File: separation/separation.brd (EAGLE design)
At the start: 5 parts, among them IC1 L7805ACV

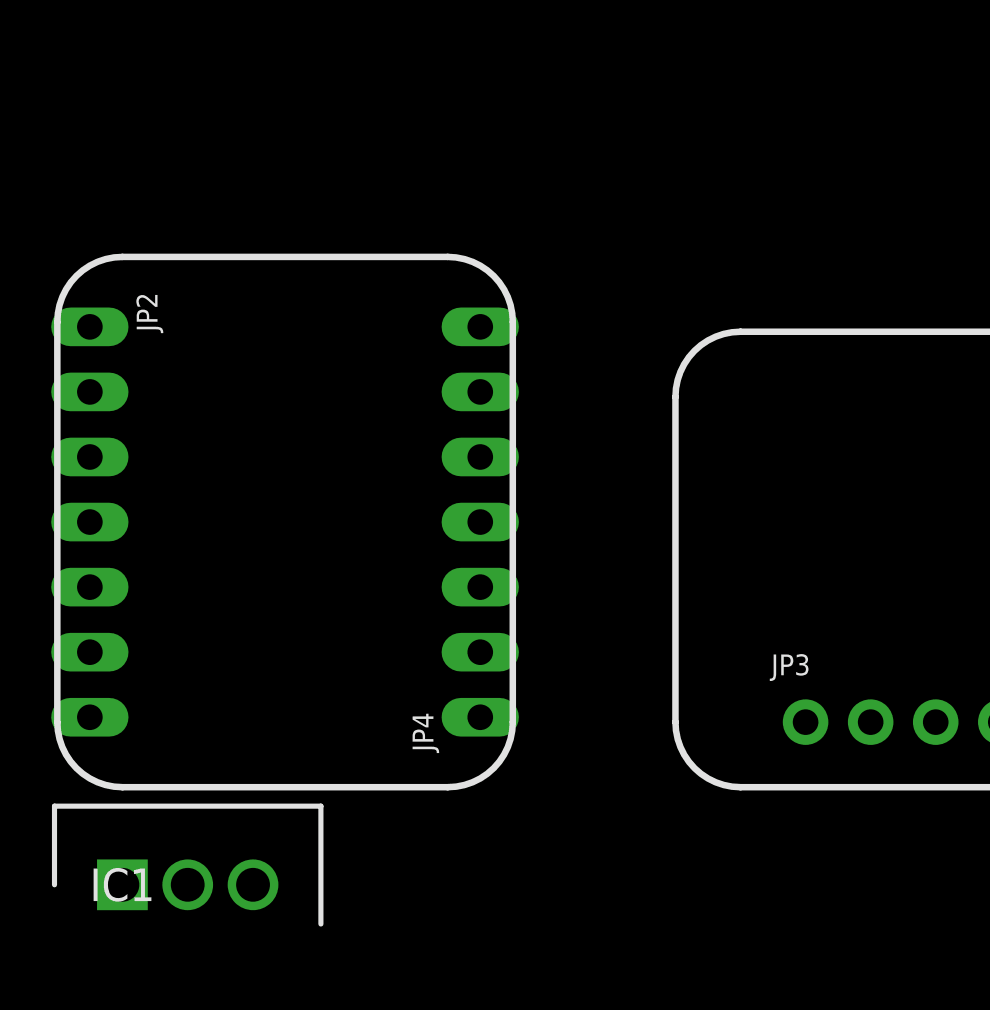
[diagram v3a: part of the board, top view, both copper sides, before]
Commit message: add buzzer
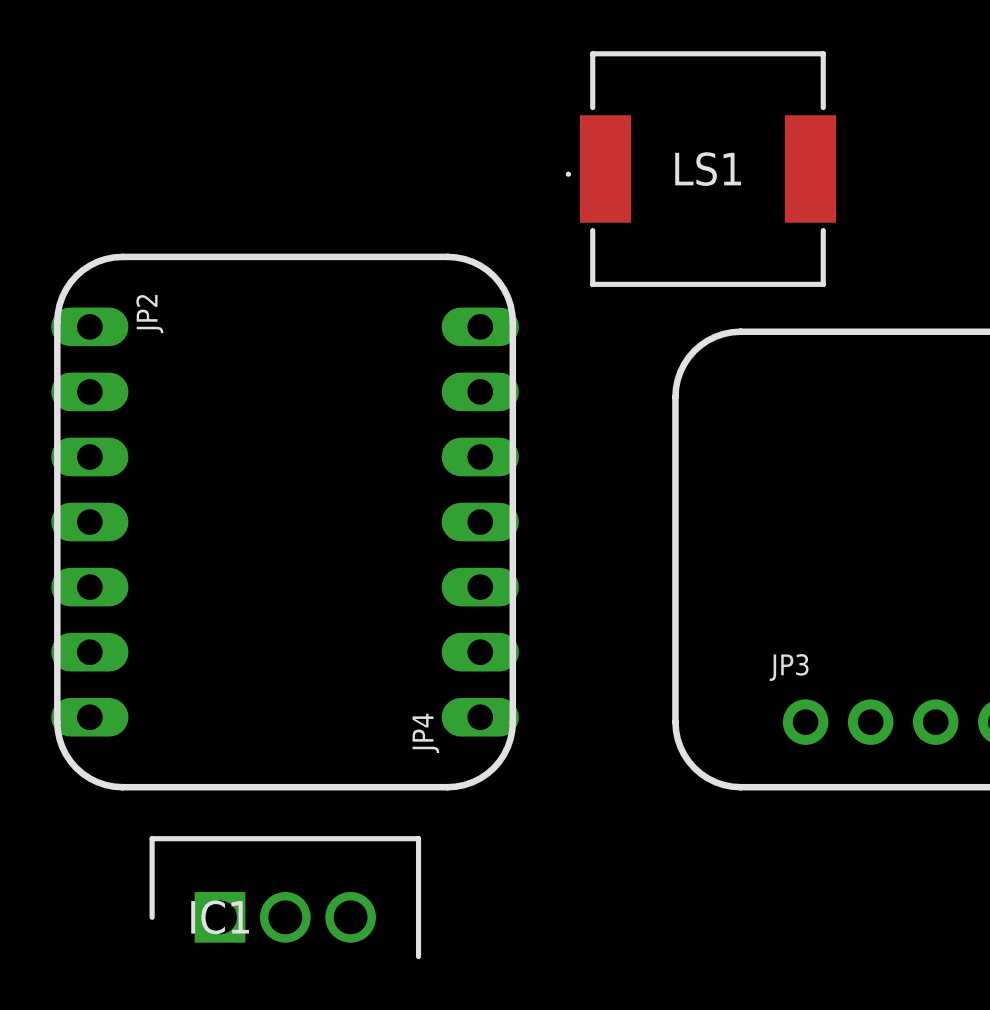
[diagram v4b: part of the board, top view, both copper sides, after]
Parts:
- added LS1: KMTG0902, SamacSys_Parts:KMTG0902
- moved IC1 4.02 mm to (44.5, 53.3)
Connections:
- net A2 renamed SERVO
- removed net A0: JP2.1
- new net BUZZ: JP2.1, LS1.1
- net GND: now also LS1.2
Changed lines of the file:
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@@
 <layer number="42" name="bRestrict" color="1" fill="10" visible="no" active="yes"/>
 <layer number="43" name="vRestrict" color="2" fill="10" visible="no" active="yes"/>
-<layer number="44" name="Drills" color="7" fill="1" visible="no" active="yes"/>
+<layer number="44" name="Drills" color="7" fill="1" visible="yes" active="yes"/>
 <layer number="45" name="Holes" color="7" fill="1" visible="yes" active="yes"/>
 <layer number="46" name="Milling" color="3" fill="1" visible="no" active="yes"/>
@@
 <attribute name="VALUE" x="93.98" y="57.785" size="0.4064" layer="27" ratio="10"/>
 </element>
-<element name="IC1" library="SamacSys_Parts" package="TO255P460X1020X2008-3P" value="L7805ACV" x="40.64" y="54.61" smashed="yes">
-<attribute name="ALLIED_NUMBER" value="70013701" x="40.64" y="54.61" size="1.778" layer="27" font="vector" ratio="15" display="off"/>
-<attribute name="DESCRIPTION" value="Linear voltage regulator,L7805ACV 5V 1A STMicroelectronics L7805ACV, Single Linear Voltage Regulator, 1A 5 V, 2%, 3-Pin TO-220" x="40.64" y="54.61" size="1.778" layer="27" font="vector" ratio="15" display="off"/>
-<attribute name="HEIGHT" value="4.6mm" x="40.64" y="54.61" size="1.778" layer="27" font="vector" ratio="15" display="off"/>
-<attribute name="MANUFACTURER_NAME" value="STMicroelectronics" x="40.64" y="54.61" size="1.778" layer="27" font="vector" ratio="15" display="off"/>
-<attribute name="MANUFACTURER_PART_NUMBER" value="L7805ACV" x="40.64" y="54.61" size="1.778" layer="27" font="vector" ratio="15" display="off"/>
-<attribute name="NAME" x="40.64" y="54.61" size="1.27" layer="25" align="center"/>
-<attribute name="RS_PART_NUMBER" value="2988508P" x="40.64" y="54.61" size="1.778" layer="27" font="vector" ratio="15" display="off"/>
-<attribute name="RS_PRICE-STOCK" value="http://uk.rs-online.com/web/p/products/2988508P" x="40.64" y="54.61" size="1.778" layer="27" font="vector" ratio="15" display="off"/>
-<attribute name="VALUE" x="40.64" y="54.61" size="1.27" layer="27" align="center"/>
+<element name="IC1" library="SamacSys_Parts" package="TO255P460X1020X2008-3P" value="L7805ACV" x="44.45" y="53.34" smashed="yes">
+<attribute name="ALLIED_NUMBER" value="70013701" x="44.45" y="53.34" size="1.778" layer="27" font="vector" ratio="15" display="off"/>
+<attribute name="DESCRIPTION" value="Linear voltage regulator,L7805ACV 5V 1A STMicroelectronics L7805ACV, Single Linear Voltage Regulator, 1A 5 V, 2%, 3-Pin TO-220" x="44.45" y="53.34" size="1.778" layer="27" font="vector" ratio="15" display="off"/>
+<attribute name="HEIGHT" value="4.6mm" x="44.45" y="53.34" size="1.778" layer="27" font="vector" ratio="15" display="off"/>
+<attribute name="MANUFACTURER_NAME" value="STMicroelectronics" x="44.45" y="53.34" size="1.778" layer="27" font="vector" ratio="15" display="off"/>
+<attribute name="MANUFACTURER_PART_NUMBER" value="L7805ACV" x="44.45" y="53.34" size="1.778" layer="27" font="vector" ratio="15" display="off"/>
+<attribute name="NAME" x="44.45" y="53.34" size="1.27" layer="25" align="center"/>
+<attribute name="RS_PART_NUMBER" value="2988508P" x="44.45" y="53.34" size="1.778" layer="27" font="vector" ratio="15" display="off"/>
+<attribute name="RS_PRICE-STOCK" value="http://uk.rs-online.com/web/p/products/2988508P" x="44.45" y="53.34" size="1.778" layer="27" font="vector" ratio="15" display="off"/>
+<attribute name="VALUE" x="44.45" y="53.34" size="1.27" layer="27" align="center"/>
+</element>
+<element name="LS1" library="SamacSys_Parts" package="KMTG0902" value="KMTG0902" x="63.5" y="82.55" smashed="yes">
+<attribute name="DESCRIPTION" value="RS PRO 65 (Minimum)dB SMD Square Wave Piezo Buzzer" x="63.5" y="82.55" size="1.778" layer="27" font="vector" ratio="15" display="off"/>
+<attribute name="HEIGHT" value="2.2mm" x="63.5" y="82.55" size="1.778" layer="27" font="vector" ratio="15" display="off"/>
+<attribute name="MANUFACTURER_NAME" value="RS Components" x="63.5" y="82.55" size="1.778" layer="27" font="vector" ratio="15" display="off"/>
+<attribute name="MANUFACTURER_PART_NUMBER" value="KMTG0902" x="63.5" y="82.55" size="1.778" layer="27" font="vector" ratio="15" display="off"/>
+<attribute name="NAME" x="63.5" y="82.55" size="1.27" layer="25" align="center"/>
+<attribute name="RS_PART_NUMBER" value="1812715" x="63.5" y="82.55" size="1.778" layer="27" font="vector" ratio="15" display="off"/>
+<attribute name="RS_PRICE-STOCK" value="https://uk.rs-online.com/web/p/products/1812715" x="63.5" y="82.55" size="1.778" layer="27" font="vector" ratio="15" display="off"/>
+<attribute name="VALUE" x="63.5" y="82.55" size="1.27" layer="27" align="center"/>
 </element>
 </elements>
@@
 <contactref element="JP6" pad="3"/>
 <contactref element="IC1" pad="2"/>
+<contactref element="LS1" pad="2"/>
 <wire x1="72.39" y1="60.96" x2="100.33" y2="60.96" width="0" layer="19" extent="1-1"/>
 <wire x1="54.61" y1="73.8505" x2="72.39" y2="60.96" width="0" layer="19" extent="1-1"/>
-<wire x1="43.19" y1="54.61" x2="54.61" y2="73.8505" width="0" layer="19" extent="1-1"/>
-</signal>
-<signal name="A0">
-<contactref element="JP2" pad="1"/>
+<wire x1="67.5" y1="82.55" x2="54.61" y2="73.8505" width="0" layer="19" extent="1-1"/>
+<wire x1="47" y1="53.34" x2="54.61" y2="73.8505" width="0" layer="19" extent="1-1"/>
 </signal>
 <signal name="A1">
@@
 <contactref element="JP4" pad="2"/>
 </signal>
-<signal name="A2">
+<signal name="SERVO">
 <contactref element="JP2" pad="3"/>
 </signal>
@@
 <wire x1="67.31" y1="60.96" x2="95.25" y2="60.96" width="0" layer="19" extent="1-1"/>
 <wire x1="54.61" y1="76.3905" x2="67.31" y2="60.96" width="0" layer="19" extent="1-1"/>
-<wire x1="45.74" y1="54.61" x2="67.31" y2="60.96" width="0" layer="19" extent="1-1"/>
+<wire x1="49.55" y1="53.34" x2="67.31" y2="60.96" width="0" layer="19" extent="1-1"/>
 </signal>
 <signal name="+3V3">
@@
 <contactref element="IC1" pad="1"/>
 </signal>
+<signal name="BUZZ">
+<contactref element="LS1" pad="1"/>
+<contactref element="JP2" pad="1"/>
+<wire x1="39.37" y1="76.3905" x2="59.5" y2="82.55" width="0" layer="19" extent="1-1"/>
+</signal>
 </signals>

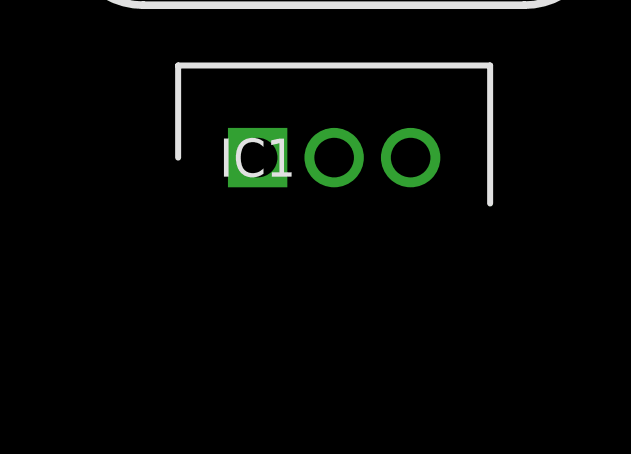
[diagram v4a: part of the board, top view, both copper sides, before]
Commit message: add servo connection
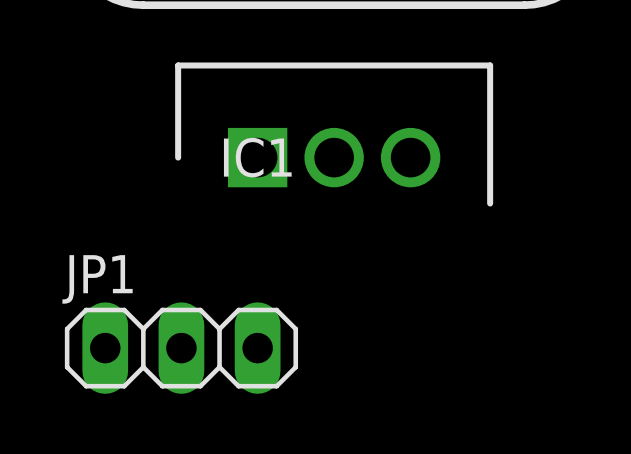
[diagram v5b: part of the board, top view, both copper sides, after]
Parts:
- added JP1: (no value), pinhead:1X03
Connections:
- net GND: now also JP1.2
- net SERVO: now also JP1.3
- net VBAT: now also JP1.1
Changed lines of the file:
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@@
 <attribute name="VALUE" x="63.5" y="82.55" size="1.27" layer="27" align="center"/>
+</element>
+<element name="JP1" library="pinhead" library_urn="urn:adsk.eagle:library:325" package="1X03" package3d_urn="urn:adsk.eagle:package:22458/2" value="" x="41.91" y="46.99" smashed="yes">
+<attribute name="NAME" x="38.0238" y="48.8188" size="1.27" layer="25" ratio="10"/>
+<attribute name="POPULARITY" value="92" x="41.91" y="46.99" size="1.778" layer="27" font="vector" ratio="15" display="off"/>
+<attribute name="VALUE" x="38.1" y="43.815" size="1.27" layer="27"/>
 </element>
 </elements>
@@
 <contactref element="IC1" pad="2"/>
 <contactref element="LS1" pad="2"/>
+<contactref element="JP1" pad="2"/>
 <wire x1="72.39" y1="60.96" x2="100.33" y2="60.96" width="0" layer="19" extent="1-1"/>
 <wire x1="54.61" y1="73.8505" x2="72.39" y2="60.96" width="0" layer="19" extent="1-1"/>
 <wire x1="67.5" y1="82.55" x2="54.61" y2="73.8505" width="0" layer="19" extent="1-1"/>
 <wire x1="47" y1="53.34" x2="54.61" y2="73.8505" width="0" layer="19" extent="1-1"/>
+<wire x1="41.91" y1="46.99" x2="47" y2="53.34" width="0" layer="19" extent="1-1"/>
 </signal>
 <signal name="A1">
@@
 <signal name="SERVO">
 <contactref element="JP2" pad="3"/>
+<contactref element="JP1" pad="3"/>
+<wire x1="44.45" y1="46.99" x2="39.37" y2="71.3105" width="0" layer="19" extent="1-1"/>
 </signal>
 <signal name="A3">
@@
 <signal name="VBAT">
 <contactref element="IC1" pad="1"/>
+<contactref element="JP1" pad="1"/>
+<wire x1="39.37" y1="46.99" x2="44.45" y2="53.34" width="0" layer="19" extent="1-1"/>
 </signal>
 <signal name="BUZZ">
@@
 </board>
 </drawing>
+<compatibility>
+<note version="8.2" severity="warning">
+Since Version 8.2, EAGLE supports online libraries. The ids
+of those online libraries will not be understood (or retained)
+with this version.
+</note>
+<note version="8.3" severity="warning">
+Since Version 8.3, EAGLE supports URNs for individual library
+assets (packages, symbols, and devices). The URNs of those assets
+will not be understood (or retained) with this version.
+</note>
+<note version="8.3" severity="warning">
+Since Version 8.3, EAGLE supports the association of 3D packages
+with devices in libraries, schematics, and board files. Those 3D
+packages will not be understood (or retained) with this version.
+</note>
+</compatibility>
 </eagle>

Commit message: basic board layout
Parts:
- added PAD1, PAD2: WIREPAD3,17/1,1, wirepad:3,17/1,1
- moved IC1 97.9 mm to (141.0, 69.8), turned to 90 degrees
- moved JP1 85.5 mm to (127.1, 54.1)
- moved LS1 83.2 mm to (143.5, 59.7)
- moved JP4 80.0 mm to (134.6, 67.5)
- moved JP2 80.0 mm to (119.4, 67.5)
- moved JP3 20.4 mm to (94.9, 65.3), turned to 90 degrees
- moved JP6 11.5 mm to (113.5, 65.2), turned to 90 degrees
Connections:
- net GND: now also PAD2.1
- net VBAT: now also PAD1.1
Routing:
- net VBAT: track 0.00 -> 38.8 mm
- net BUZZ: track 0.00 -> 37.7 mm, vias 0 -> 2
- net SDA: track 0.00 -> 28.2 mm
- net SCL: track 0.00 -> 25.9 mm
- net SERVO: track 0.00 -> 23.8 mm

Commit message: remove all 3v3 lines
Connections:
- removed net +3V3: JP4.5
- removed net 3.3V: JP3.2, JP6.2
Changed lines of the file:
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@@
 <wire x1="140.97" y1="74.95" x2="94.869" y2="57.658" width="0" layer="19" extent="1-1"/>
-</signal>
-<signal name="+3V3">
-<contactref element="JP4" pad="5"/>
 </signal>
 <signal name="PB22/I6/SERCOM5.1">
@@
 <contactref element="JP4" pad="1"/>
 </signal>
-<signal name="3.3V" class="2">
-<contactref element="JP3" pad="2"/>
-<contactref element="JP6" pad="2"/>
-<wire x1="94.869" y1="60.198" x2="113.538" y2="60.071" width="0" layer="19" extent="1-1"/>
-</signal>
 <signal name="SDO/ADR">

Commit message: remove cs lines
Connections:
- removed net CS: JP3.7, JP6.7
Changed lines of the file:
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@@
 <contactref element="JP3" pad="5"/>
-</signal>
-<signal name="CS">
-<contactref element="JP3" pad="7"/>
-<contactref element="JP6" pad="7"/>
-<wire x1="94.869" y1="72.898" x2="113.538" y2="72.771" width="0" layer="19" extent="1-1"/>
 </signal>
 <signal name="SDO/ADR_2">
